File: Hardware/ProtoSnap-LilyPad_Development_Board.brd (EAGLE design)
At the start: 104.1 x 72.4 mm, 156 parts, among them M1 MOTORSMD, U1 ATMEGA328, U2 MCP9700, U3 TEMT6000, U4 MCP73831, Y1 8MHz

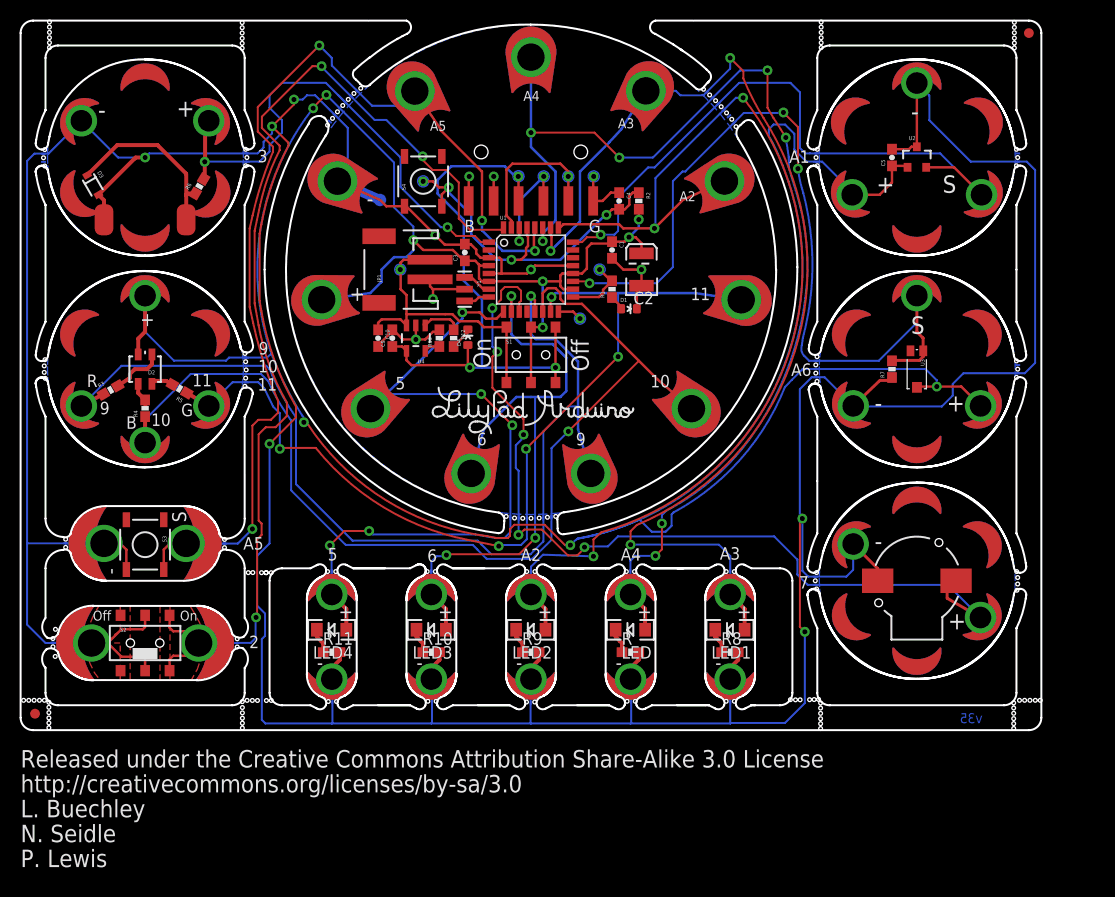
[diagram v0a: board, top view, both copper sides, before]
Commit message: finishing up v35 - a few things
-updated LILYPAD-BRD-LAYERS.pac to include fixed polygons.
-updated to ledger in schematic, updated "designed by" text objects.
re-spaced schematic for more even look
-updated to 1:1 (+fake traces) footprint on resonator package
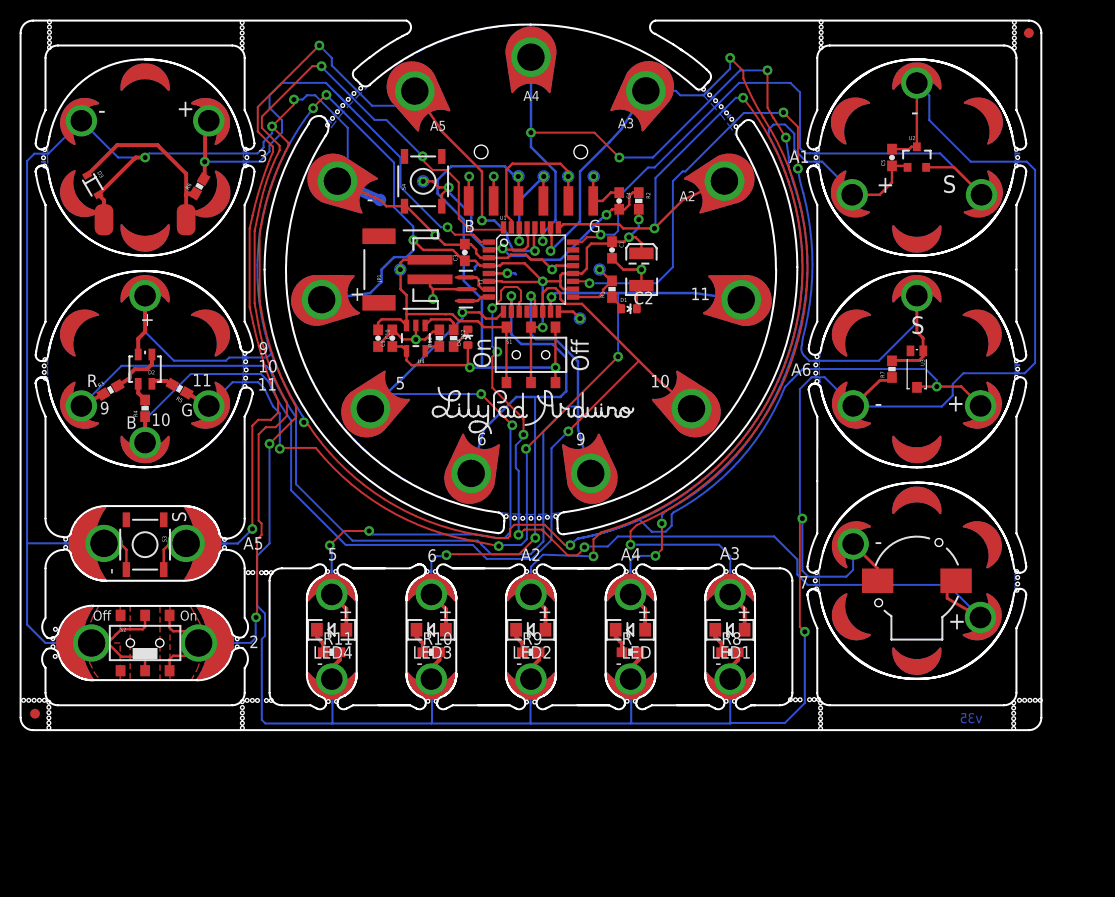
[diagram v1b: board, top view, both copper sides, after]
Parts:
- added FRAME2: FRAME-LEDGER, SparkFun-Aesthetics:CREATIVE_COMMONS
- Y1: device SparkFun:RESONATOR-SMD -> Testing:RESONATOR-SMD-1:1
- moved Y1 0.13 mm to (45.4, 45.0)
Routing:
- net VCC: track 300.1 -> 304.0 mm
- net GND: track 463.5 -> 464.9 mm, vias 13 -> 14
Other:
- board text removed: "Released under the Creative Commons Attribution Share-Alike 3.0 License"
- board text removed: "http://creativecommons.org/licenses/by-sa/3.0"

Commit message: Added diode from VBATT to VBUS
also updated to flags in schematic.
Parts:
- added D5: B340A, SparkFun-DiscreteSemi:SMA-DIODE
- D1, D4: device SparkFun-LED:LED-0603-QC -> Testing:0603-LED-ALT1
- S4: device SparkFun:TACTILE_SWITCH_SMD -> Testing:TACTILE-SWITCH-SMD-ALT01
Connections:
- removed net N$12: U1.2
- removed net N$14: U1.12
- removed net N$5: U1.23
- removed net N$8: U1.22
- net FTDI_VCC: now also D5.C
- net GND: now also S4.2
- net RST: now also S4.4
- net VBATT: now also D5.A
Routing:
- net VBATT: track 31.0 -> 42.9 mm, vias 1 -> 3
- net GND: track 464.9 -> 470.7 mm
- net D5: track 68.4 -> 63.6 mm
- net RST: track 37.5 -> 40.8 mm
- net D2: track 109.0 -> 111.8 mm
- net FTDI_VCC: track 58.9 -> 60.6 mm, vias 3 -> 4
- net N$2: track 1.54 -> 2.43 mm
